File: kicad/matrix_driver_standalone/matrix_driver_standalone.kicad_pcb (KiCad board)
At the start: 4 copper layers, 20 x 22 mm, 17 parts, among them J1 Conn_01x04, J2 Conn_01x04, U1 IS31FL3743A

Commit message: minor PCB fixes - display led matrix, standalone driver module
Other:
- board text added: "1"
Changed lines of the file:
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@@
 			(outputformat 1)
 			(mirror no)
-			(drillshape 1)
+			(drillshape 0)
 			(scaleselection 1)
-			(outputdirectory "")
+			(outputdirectory "matrix_driver_standalone_gerbers/")
 		)
 	)
@@
 		(tags "capacitor")
 		(property "Reference" "C5"
-			(at 0 -1.43 45)
+			(at -0.845711 -1.202082 45)
 			(layer "F.SilkS")
 			(effects
 				(font
-					(size 1 1)
+					(size 0.8 0.8)
 					(thickness 0.15)
 				)
@@
 		(tags "capacitor")
 		(property "Reference" "C4"
-			(at 0 -1.43 135)
+			(at 0.282843 -1.272792 135)
 			(layer "F.SilkS")
 			(effects
 				(font
-					(size 1 1)
+					(size 0.8 0.8)
 					(thickness 0.15)
 				)
@@
 		(tags "Through hole pin header THT 1x04 2.54mm single row")
 		(property "Reference" "J1"
-			(at 0 -2.38 90)
+			(at -1.4 -4.187 90)
 			(layer "F.SilkS")
+			(hide yes)
 			(effects
 				(font
@@
 		(tags "solder jumper open")
 		(property "Reference" "JP2"
-			(at 0 -1.8 90)
+			(at -3.4 0.5 90)
 			(layer "F.SilkS")
 			(effects
 				(font
-					(size 1 1)
+					(size 0.8 0.8)
 					(thickness 0.15)
 				)
@@
 		(tags "resistor")
 		(property "Reference" "R4"
-			(at 0 -1.43 90)
+			(at 0 1.4 90)
 			(layer "F.SilkS")
 			(effects
 				(font
-					(size 1 1)
+					(size 0.8 0.8)
 					(thickness 0.15)
 				)
@@
 		(tags "resistor")
 		(property "Reference" "R6"
-			(at 0 -1.43 45)
+			(at -0.094239 -2.899138 45)
 			(layer "F.SilkS")
 			(effects
 				(font
-					(size 1 1)
+					(size 0.8 0.8)
 					(thickness 0.15)
 				)
@@
 		(tags "resistor")
 		(property "Reference" "R3"
-			(at 0 -1.43 45)
+			(at 0.094239 -2.899138 45)
 			(layer "F.SilkS")
 			(effects
 				(font
-					(size 1 1)
+					(size 0.8 0.8)
 					(thickness 0.15)
 				)
@@
 		(tags "resistor")
 		(property "Reference" "R1"
-			(at 0 -1.43 90)
+			(at 2.2 0.3 90)
 			(layer "F.SilkS")
 			(effects
 				(font
-					(size 1 1)
+					(size 0.8 0.8)
 					(thickness 0.15)
 				)
@@
 		(tags "resistor")
 		(property "Reference" "R2"
-			(at 0 -1.43 90)
+			(at 2.2 0.1 90)
 			(layer "F.SilkS")
 			(effects
 				(font
-					(size 1 1)
+					(size 0.8 0.8)
 					(thickness 0.15)
 				)
@@
 		(tags "capacitor")
 		(property "Reference" "C3"
-			(at 0 -1.43 135)
+			(at 0.707107 1.272792 135)
 			(layer "F.SilkS")
 			(effects
 				(font
-					(size 1 1)
+					(size 0.8 0.8)
 					(thickness 0.15)
 				)
@@
 			(at 0 -2.38 90)
 			(layer "F.SilkS")
+			(hide yes)
 			(effects
 				(font
@@
 		(tags "capacitor")
 		(property "Reference" "C2"
-			(at 0 -1.43 135)
+			(at 2.474874 -0.212132 135)
 			(layer "F.SilkS")
 			(effects
 				(font
-					(size 1 1)
+					(size 0.8 0.8)
 					(thickness 0.15)
 				)
@@
 		(tags "solder jumper open")
 		(property "Reference" "JP1"
-			(at 0 -1.8 90)
+			(at 3.8 0.5 90)
 			(layer "F.SilkS")
 			(effects
 				(font
-					(size 1 1)
+					(size 0.8 0.8)
 					(thickness 0.15)
 				)
@@
 		(at 131.9 78.8 45)
 		(property "Reference" "U1"
-			(at 0.3 3.8 45)
+			(at 0.212132 3.606245 45)
 			(unlocked yes)
 			(layer "F.SilkS")
 			(effects
 				(font
-					(size 1 1)
+					(size 0.8 0.8)
 					(thickness 0.1)
 				)
@@
 		(tags "capacitor")
 		(property "Reference" "C1"
-			(at 0 -1.43 135)
+			(at 2.474874 -0.494975 135)
 			(layer "F.SilkS")
 			(effects
 				(font
-					(size 1 1)
+					(size 0.8 0.8)
 					(thickness 0.15)
 				)
@@
 		(tags "resistor")
 		(property "Reference" "R5"
-			(at 0 -1.43 90)
+			(at 0 -1.4 90)
 			(layer "F.SilkS")
 			(effects
 				(font
-					(size 1 1)
+					(size 0.8 0.8)
 					(thickness 0.15)
 				)
@@
 		)
 		(group ""
-			(members "170a7268-bd29-4360-9817-e61b46a28046" "277cbfda-7dd3-4638-b017-0455d26b3874"
-				"3988b7ef-b0bb-4f6b-8b2c-14aead69893b" "3a6d7e4b-a108-4c78-b1fe-eb6ec4ecf3dc"
-				"63c729fc-67e2-45b9-9c3f-95ff4f177f14" "8b6d13fd-fab0-4c21-b93f-7248d89d2aca"
-				"9437031e-3d38-429b-ae80-4f69fbbd7252" "ae44a786-a692-4a46-99f4-7a3f972f1947"
-				"b8227805-9266-4dea-a996-b9f648a08306" "e93354db-a115-4acf-9c35-c5b40f9aa267"
-				"f851f981-1cf0-41ec-a2c0-118b1532dfa3" "fec1b5dc-a937-4f4d-b488-8f9518cb913f"
+			(members "14755828-87e4-486f-acbd-65c9e524960d" "14e49a68-7066-4c25-aa33-d755dccc3f12"
+				"170a7268-bd29-4360-9817-e61b46a28046" "362f7080-cf8f-430d-b7d8-c981acbb5c2b"
+				"3a227052-870d-4e93-a28a-846ac23bc74a" "63349daf-fb85-43d3-9f83-ddb0b3b753e8"
+				"75f5b3f1-b02a-47b5-a74a-cd642b8edcc5" "9d7052e4-bb0d-4591-ad5d-b171ec1c3257"
+				"ae44a786-a692-4a46-99f4-7a3f972f1947" "c9c2a440-9aa2-485a-b6d8-dbd5d1f25464"
+				"e9717a05-2d2a-4a8d-928c-9703f97de357" "fec1b5dc-a937-4f4d-b488-8f9518cb913f"
 			)
 		)
@@
 		)
 		(embedded_fonts no)
+		(model "/home/michael/sync/projects/emes/kicad/display_matrix/display_matrix.step"
+			(opacity 0.4100)
+			(offset
+				(xyz -0.3 0 0)
+			)
+			(scale
+				(xyz 1 1 1)
+			)
+			(rotate
+				(xyz -0 -0 -0)
+			)
+		)
 	)
 	(gr_line
@@
 		(layer "Edge.Cuts")
 	)
+	(gr_text "1"
+		(at 125.2 68.8 180)
+		(layer "B.SilkS")
+		(effects
+			(font
+				(size 1 1)
+				(thickness 0.1)
+			)
+			(justify left bottom mirror)
+		)
+	)
 	(segment

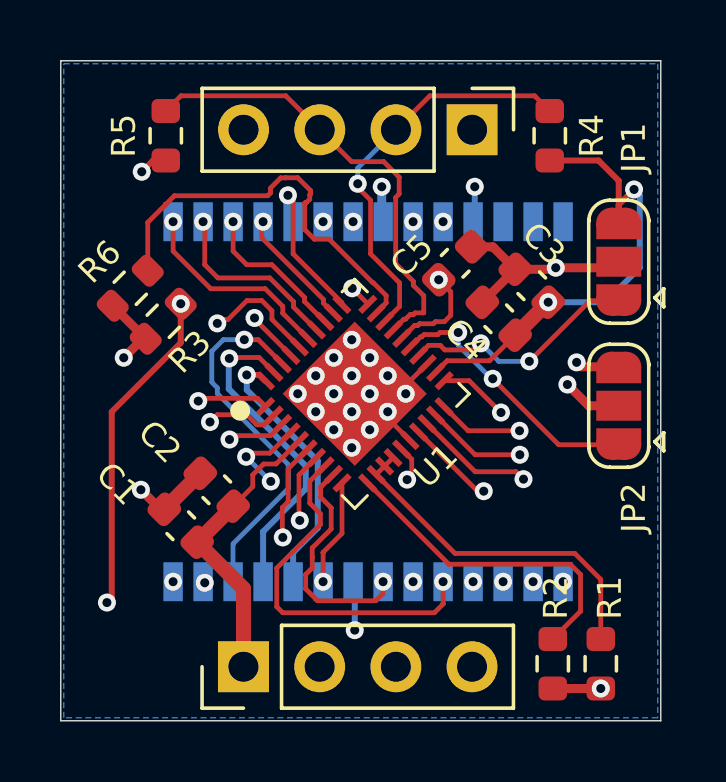
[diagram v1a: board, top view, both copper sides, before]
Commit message: play bad apple; fix an oopsie in the driver schematics/pcb
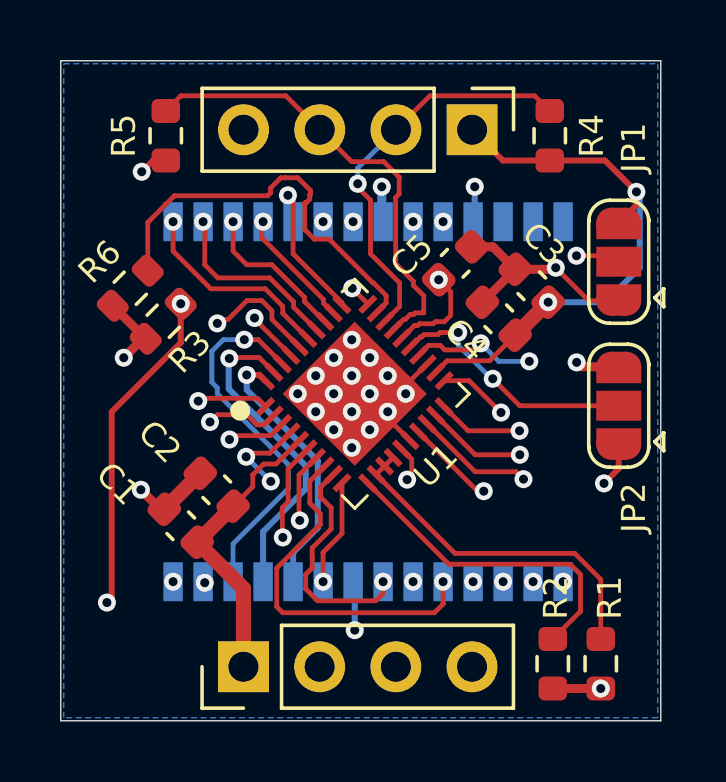
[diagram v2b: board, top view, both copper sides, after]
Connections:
- JP1 pad 1: Net-(JP1-A) -> GND
- JP1 pad 2: GND -> Net-(JP1-C)
- JP2 pad 1: Net-(JP2-A) -> GND
- JP2 pad 2: GND -> Net-(JP2-C)
- U1 pad 24: Net-(JP1-A) -> Net-(JP1-C)
- U1 pad 25: Net-(JP2-A) -> Net-(JP2-C)
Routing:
- net Net-(JP1-C): track 0.00 -> 10.2 mm, vias 0 -> 3
- net Net-(JP2-A): track 8.95 -> 0.00 mm, vias 2 -> 0
- net Net-(JP2-C): track 0.00 -> 8.41 mm, vias 0 -> 2
- net Net-(JP1-A): track 8.04 -> 0.00 mm, vias 2 -> 0
- net VCC: track 72.1 -> 67.1 mm
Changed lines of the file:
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@@
 	(net 4 "SDA")
 	(net 5 "SYNC")
-	(net 6 "Net-(JP1-A)")
-	(net 7 "Net-(JP2-A)")
+	(net 6 "Net-(JP1-C)")
+	(net 7 "Net-(JP2-C)")
 	(net 8 "Net-(U1-CS16)")
 	(net 9 "Net-(U1-SW11)")
@@
 			(size 1 0.5)
 			(layers "F.Cu" "F.Mask")
-			(net 7 "Net-(JP2-A)")
+			(net 2 "GND")
 			(pinfunction "A")
 			(pintype "passive")
@@
 			(size 1 1.5)
 			(layers "F.Cu" "F.Mask")
-			(net 2 "GND")
+			(net 7 "Net-(JP2-C)")
 			(pinfunction "C")
 			(pintype "passive")
@@
 			(size 1 0.5)
 			(layers "F.Cu" "F.Mask")
-			(net 6 "Net-(JP1-A)")
+			(net 2 "GND")
 			(pinfunction "A")
 			(pintype "passive")
@@
 			(size 1 1.5)
 			(layers "F.Cu" "F.Mask")
-			(net 2 "GND")
+			(net 6 "Net-(JP1-C)")
 			(pinfunction "C")
 			(pintype "passive")
@@
 			(size 0.715 0.2)
 			(layers "F.Cu" "F.Mask" "F.Paste")
-			(net 6 "Net-(JP1-A)")
+			(net 6 "Net-(JP1-C)")
 			(pinfunction "ADDR2")
 			(pintype "input")
@@
 			(size 0.715 0.2)
 			(layers "F.Cu" "F.Mask" "F.Paste")
-			(net 7 "Net-(JP2-A)")
+			(net 7 "Net-(JP2-C)")
 			(pinfunction "ADDR1")
 			(pintype "input")
@@
 	)
 	(segment
+		(start 141.28962 72.51038)
+		(end 140.7 73.1)
+		(width 0.2)
+		(layer "F.Cu")
+		(net 1)
+	)
+	(segment
 		(start 128.860341 81.141311)
 		(end 128.5 81.501652)
@@
 	)
 	(segment
-		(start 138.348008 75.751992)
-		(end 137.2 76.9)
-		(width 0.5)
+		(start 141.28962 72.07038)
+		(end 141.28962 72.51038)
+		(width 0.2)
 		(layer "F.Cu")
 		(net 1)
 	)
 	(segment
-		(start 140.025 71.025)
-		(end 138.4 71.025)
-		(width 0.2)
+		(start 138.348008 75.751992)
+		(end 137.2 76.9)
+		(width 0.5)
 		(layer "F.Cu")
 		(net 1)
@@
 	)
 	(segment
-		(start 140.7 73.1)
-		(end 140.7 72.5)
-		(width 0.2)
-		(layer "F.Cu")
-		(net 1)
-	)
-	(segment
 		(start 136.396016 77.7)
 		(end 137.248008 76.848008)
@@
 	)
 	(segment
-		(start 140.025 71.025)
-		(end 140.7 71.7)
+		(start 138.4 71.025)
+		(end 136.838 71.025)
+		(width 0.2)
+		(layer "F.Cu")
+		(net 1)
+	)
+	(segment
+		(start 140.24424 71.025)
+		(end 138.4 71.025)
 		(width 0.2)
 		(layer "F.Cu")
@@
 	)
 	(segment
-		(start 140.7 71.7)
-		(end 140.7 73.1)
+		(start 141.28962 72.07038)
+		(end 140.24424 71.025)
 		(width 0.2)
 		(layer "F.Cu")
@@
 	)
 	(segment
-		(start 140.7 72.5)
-		(end 141.20962 71.99038)
+		(start 136.838 71.025)
+		(end 135.813 70)
 		(width 0.2)
 		(layer "F.Cu")
@@
 	)
 	(via
-		(at 141.20962 71.99038)
+		(at 124.8 71.4)
 		(size 0.6)
 		(drill 0.3)
@@
 	)
 	(via
-		(at 124.8 71.4)
+		(at 141.28962 72.07038)
 		(size 0.6)
 		(drill 0.3)
@@
 	)
 	(segment
-		(start 140.251992 75.748008)
-		(end 138.348008 75.748008)
+		(start 141.4 72.18076)
+		(end 141.28962 72.07038)
 		(width 0.2)
 		(layer "B.Cu")
@@
 	)
 	(segment
-		(start 141.4 74.6)
-		(end 140.251992 75.748008)
+		(start 140.251992 75.748008)
+		(end 138.348008 75.748008)
 		(width 0.2)
 		(layer "B.Cu")
@@
 	)
 	(segment
-		(start 141.20962 71.99038)
-		(end 141.4 72.18076)
+		(start 141.4 74.6)
+		(end 140.251992 75.748008)
 		(width 0.2)
 		(layer "B.Cu")
@@
 	)
 	(segment
-		(start 138.07024 68.851)
-		(end 141.20962 71.99038)
-		(width 0.3)
-		(layer "In1.Cu")
-		(net 1)
-	)
-	(segment
-		(start 138.07024 68.851)
-		(end 136.962 68.851)
-		(width 0.3)
-		(layer "In1.Cu")
-		(net 1)
-	)
-	(segment
-		(start 136.962 68.851)
-		(end 135.813 70)
-		(width 0.3)
-		(layer "In1.Cu")
-		(net 1)
-	)
-	(segment
 		(start 128.19 87.9)
 		(end 126.84 87.9)
@@
 	)
 	(segment
-		(start 140.5 74.6)
-		(end 140.7 74.4)
-		(width 0.3)
+		(start 139.7 75.7)
+		(end 138.6 74.6)
+		(width 0.16)
+		(layer "F.Cu")
+		(net 2)
+	)
+	(segment
+		(start 140.7 75.7)
+		(end 139.7 75.7)
+		(width 0.16)
 		(layer "F.Cu")
 		(net 2)
@@
 	)
 	(segment
-		(start 139.696 79.2)
-		(end 138.98838 78.49238)
-		(width 0.3)
+		(start 140.7 81.296)
+		(end 140.208 81.788)
+		(width 0.2)
 		(layer "F.Cu")
 		(net 2)
@@
 	)
 	(segment
-		(start 140.7 79.2)
-		(end 139.696 79.2)
-		(width 0.3)
-		(layer "F.Cu")
-		(net 2)
-	)
-	(segment
-		(start 138.6 74.6)
-		(end 140.5 74.6)
-		(width 0.3)
-		(layer "F.Cu")
-		(net 2)
-	)
-	(segment
 		(start 125.423445 82.651992)
 		(end 124.771453 82)
@@
 		(net 2)
 	)
+	(segment
+		(start 140.7 80.5)
+		(end 140.7 81.296)
+		(width 0.2)
+		(layer "F.Cu")
+		(net 2)
+	)
 	(via
 		(at 131.2 77.6)
@@
 	)
 	(via
-		(at 138.98838 78.49238)
+		(at 132.4 80)
 		(size 0.6)
 		(drill 0.3)
@@
 	)
 	(via
-		(at 132.4 80)
+		(at 131.8 80.6)
 		(size 0.6)
 		(drill 0.3)
@@
 	)
 	(via
-		(at 131.8 80.6)
+		(at 124.771453 82)
 		(size 0.6)
 		(drill 0.3)
@@
 	)
 	(via
-		(at 124.771453 82)
+		(at 140.208 81.788)
 		(size 0.6)
 		(drill 0.3)
@@
 	)
 	(segment
-		(start 134.031927 77.516601)
-		(end 134.360656 77.187872)
+		(start 139.292661 74.199722)
+		(end 140.499722 74.199722)
 		(width 0.16)
 		(layer "F.Cu")
@@
 	)
 	(segment
-		(start 134.748872 77.187872)
-		(end 134.9 77.339)
+		(start 140.5 74.6)
+		(end 140.7 74.4)
+		(width 0.3)
+		(layer "F.Cu")
+		(net 6)
+	)
+	(segment
+		(start 140.499722 74.199722)
+		(end 140.7 74.4)
 		(width 0.16)
 		(layer "F.Cu")
@@
 	)
 	(segment
-		(start 139.739338 75.7)
-		(end 140.7 75.7)
+		(start 134.031927 77.516601)
+		(end 134.360656 77.187872)
 		(width 0.16)
 		(layer "F.Cu")
@@
 	)
 	(segment
-		(start 137.719224 77.720114)
-		(end 139.739338 75.7)
+		(start 134.748872 77.187872)
+		(end 134.9 77.339)
 		(width 0.16)
 		(layer "F.Cu")
@@
 		(net 6)
 	)
+	(via
+		(at 139.292661 74.199722)
+		(size 0.6)
+		(drill 0.3)
+		(layers "F.Cu" "B.Cu")
+		(net 6)
+	)
 	(segment
 		(start 136.1 77.12)
@@
 	)
 	(segment
+		(start 139.292661 76.146677)
+		(end 139.292661 74.199722)
+		(width 0.16)
+		(layer "In1.Cu")
+		(net 6)
+	)
+	(segment
+		(start 137.719224 77.720114)
+		(end 139.292661 76.146677)
+		(width 0.16)
+		(layer "In1.Cu")
+		(net 6)
+	)
+	(segment
 		(start 134.132967 76.905029)
 		(end 134.090541 76.905029)
@@
 	)
 	(segment
-		(start 138.7 80.5)
-		(end 140.7 80.5)
+		(start 134.090541 76.905029)
+		(end 133.89557 77.1)
 		(width 0.16)
 		(layer "F.Cu")
@@
 	)
 	(segment
-		(start 134.090541 76.905029)
-		(end 133.89557 77.1)
+		(start 136.5 78.3)
+		(end 137.4 79.2)
 		(width 0.16)
 		(layer "F.Cu")
@@
 	)
 	(segment
-		(start 136.5 78.3)
-		(end 138.7 80.5)
+		(start 134.741 76.759)
+		(end 134.673128 76.826872)
 		(width 0.16)
 		(layer "F.Cu")
@@
 	)
 	(segment
-		(start 134.741 76.759)
-		(end 134.673128 76.826872)
+		(start 134.211124 76.826872)
+		(end 134.132967 76.905029)
 		(width 0.16)
 		(layer "F.Cu")
@@
 	)
 	(segment
-		(start 134.211124 76.826872)
-		(end 134.132967 76.905029)
+		(start 137.4 79.2)
+		(end 140.7 79.2)
 		(width 0.16)
 		(layer "F.Cu")
